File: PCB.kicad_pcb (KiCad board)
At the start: 2 copper layers, 60 x 60 mm, 51 parts, among them J1 USB_C_Receptacle_USB2.0_16P, J10 Conn_01x06_Socket, J11 Conn_01x02_Pin, J13 Conn_01x06_Pin, J2 Conn_01x06_Socket, J3 Conn_01x04_Pin, J4 Conn_01x06_Pin, J5 Conn_01x02_Pin, J6 Conn_01x02_Pin, J7 Conn_01x02_Pin, J8 Conn_01x04_Pin, J9 Conn_01x06_Pin, SW1 SW_Push, SW2 SW_Push, U1 TMC2209_SILENTSTEPSTICK, U2 USBLC6-2SC6, U4 AMS1117-3.3 (UMW), U5 TMC2209_SILENTSTEPSTICK, U6 ESP32-S3-WROOM-1

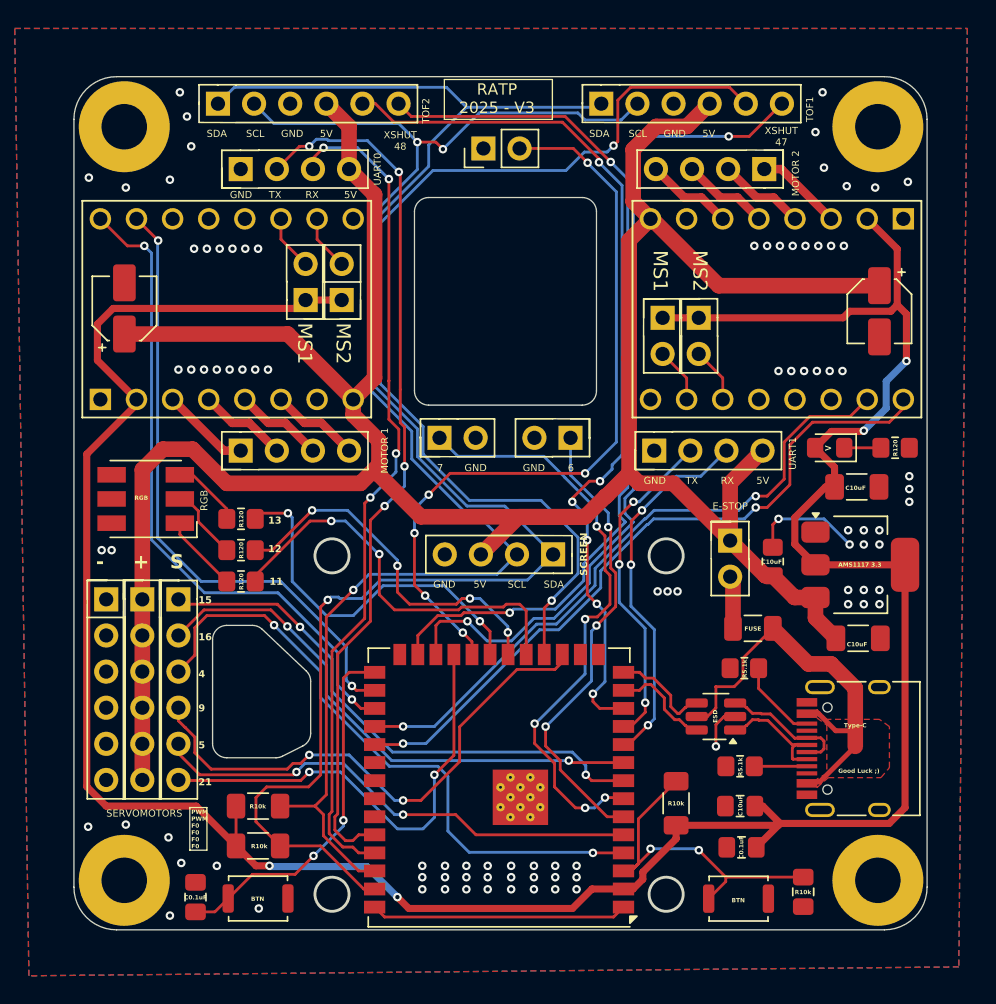
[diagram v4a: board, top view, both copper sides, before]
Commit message: fin routage + faire Trou Screen gnd
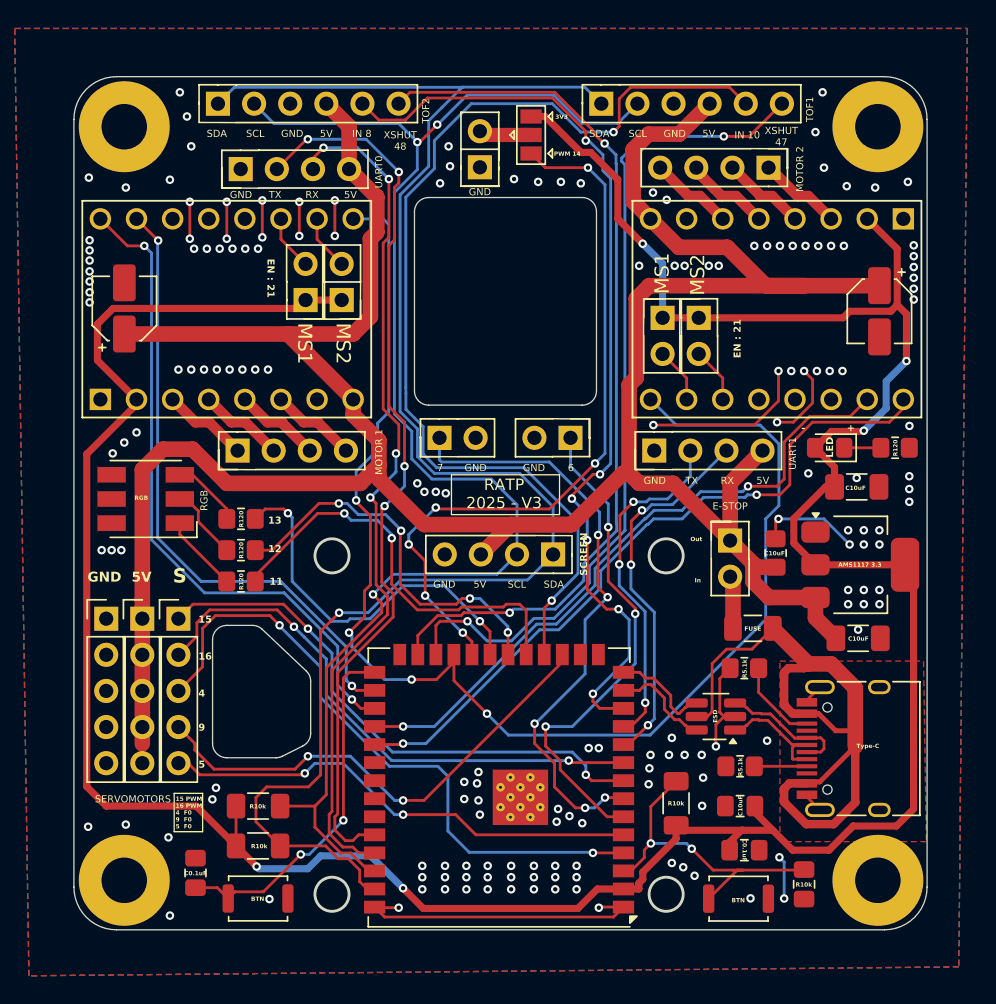
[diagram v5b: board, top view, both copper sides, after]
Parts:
- added JP5: SolderJumper_3_Open, Jumper:SolderJumper-3_P1.3mm_Open_Pad1.0x1.5mm, F.Cu at (145.4, 75.6)
- J13, J4, J9: value Conn_01x06_Pin -> Conn_01x05_Pin; footprint Connector_PinHeader_2.54mm:PinHeader_1x06_P2.54mm_Vertical -> Connector_PinHeader_2.54mm:PinHeader_1x05_P2.54mm_Vertical
- moved C1 1.70 mm to (121.8, 127.5)
- moved J13 1.36 mm to (115.5, 109.6)
- moved J4 1.36 mm to (120.6, 109.6)
- moved J9 1.36 mm to (118.1, 109.6)
- moved J11 1.35 mm to (141.8, 77.9), turned to 180 degrees
- moved C4 0.63 mm to (162.6, 105.0)
- moved C2 0.53 mm to (164.6, 128.3)
- moved J3 0.32 mm to (162.1, 77.9)
- moved C10 0.28 mm to (160.4, 125.9), turned to 0 degrees
- moved J8 0.22 mm to (124.8, 97.8)
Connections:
- J11 pad 2: GPIO14_PWM -> Net-(J11-Pin_2)
- U1 pad 16: GND -> GPIO21
- U5 pad 16: GND -> GPIO21
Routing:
- net GPIO21: track 32.3 -> 95.6 mm, vias 2 -> 4
- net GND: track 29.4 -> 72.8 mm, vias 93 -> 171
- net 3V3: track 198.2 -> 220.2 mm, vias 4 -> 5
- net VCC_5Vin: track 29.2 -> 48.0 mm
- net VCC_5V: track 192.1 -> 197.9 mm
- net Net-(J11-Pin_2): track 0.00 -> 3.71 mm
- net GPIO8: track 62.6 -> 65.7 mm
- net GPIO9: track 37.7 -> 34.7 mm
- net GPIO14_PWM: track 53.9 -> 51.7 mm
- net LAUNCHPULL: track 33.0 -> 35.2 mm
- net GPIO10: track 71.9 -> 73.3 mm
- net GPIO12_PWM: track 25.9 -> 27.3 mm
- net GPIO16_PWM: track 37.7 -> 39.1 mm
- net UART0+: track 59.6 -> 60.9 mm
- net UART0-: track 62.2 -> 63.4 mm
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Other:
- board text added: "15 PWM 16 PWM 4 F0 9 F0 5 F0"
- board text added: "3V3"
- board text added: "EN : 21"
- board text added: "IN 10"
- board text added: "IN 8"
- board text added: "In"
- board text added: "LED"
- board text added: "Out"
- board text added: "PWM 14"
- board text removed: "21"
- board text removed: ">"
- board text removed: "Good Luck ;)"
- board text removed: "PWM PWM F0 F0 F0 F0"

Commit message: test DRC V3 OK prod
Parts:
- C7: value 10uF -> 22uF
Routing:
- net GND: track 72.8 -> 97.8 mm, vias 171 -> 192
- net ESP32_EN: track 23.0 -> 27.2 mm
- net 3V3: track 220.2 -> 221.4 mm
- net VCC_5V: track 197.9 -> 198.9 mm
- net LAUNCHPULL: track 35.2 -> 34.4 mm
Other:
- board text added: "C100uF"
- board text added: "C22uF"
- board text added: "Check short circuit !"
- board text added: "Chicken Jockey"
- board text added: "Flint & Steel"
- board text added: "I AM STEVE"
- board text added: "POWER SUPPLY : PD Control 5V/3A POWER SUPPLY : using E-Stop MAX 3A STEPPER : MAX 2.40A/Phase +20°C UART : wired like TX on TX & RX on RX FUSE PPTC: hold 3A & drop 3.5A MULTI BOARD : use UART0 or UART1 UART0 : DON'T USE when flashing"
- board text added: "Unimakers Amiens"

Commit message: V3 Corrigée (ToF)
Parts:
- C7: value 22uF -> 10uF
- moved JP5 0.86 mm to (145.5, 76.5)
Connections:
- J10 pad 1: SDA -> VCC_5V
- J10 pad 2: SCL -> GND
- J10 pad 3: GND -> SCL
- J10 pad 4: VCC_5V -> SDA
- J2 pad 1: SDA -> VCC_5V
- J2 pad 2: SCL -> GND
- J2 pad 3: GND -> SCL
- J2 pad 4: VCC_5V -> SDA
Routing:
- net VCC_5V: track 198.9 -> 202.4 mm
- net GND: track 97.8 -> 100.4 mm, vias 192 -> 191
- net GPIO10: track 73.3 -> 71.0 mm
- net Net-(J11-Pin_2): track 3.71 -> 4.54 mm
- net SDA: track 117.0 -> 116.3 mm, vias 1 -> 2
- net XSHUT1: track 58.7 -> 58.2 mm, vias 2 -> 1
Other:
- board text added: "FUSE PPTC:hold 3A & drop 3.5A MULTI BOARD:use UART0/UART1 UART0:DON'T USE when flashing"
- board text added: "POWER SUPPLY:PD Control 5V/3A POWER SUPPLY:E-Stop MAX 3A STEPPER:MAX 2.40A/Phase +20°C UART:wired TX on TX/RX on RX FUSE PPTC:hold 3A&drop 3.5A"
- board text removed: "Chicken Jockey"
- board text removed: "Flint & Steel"
- board text removed: "I AM STEVE"
- board text removed: "POWER SUPPLY : PD Control 5V/3A POWER SUPPLY : using E-Stop MAX 3A STEPPER : MAX 2.40A/Phase +20°C UART : wired like TX on TX & RX on RX FUSE PPTC: hold 3A & drop 3.5A MULTI BOARD : use UART0 or UART1 UART0 : DON'T USE when flashing"

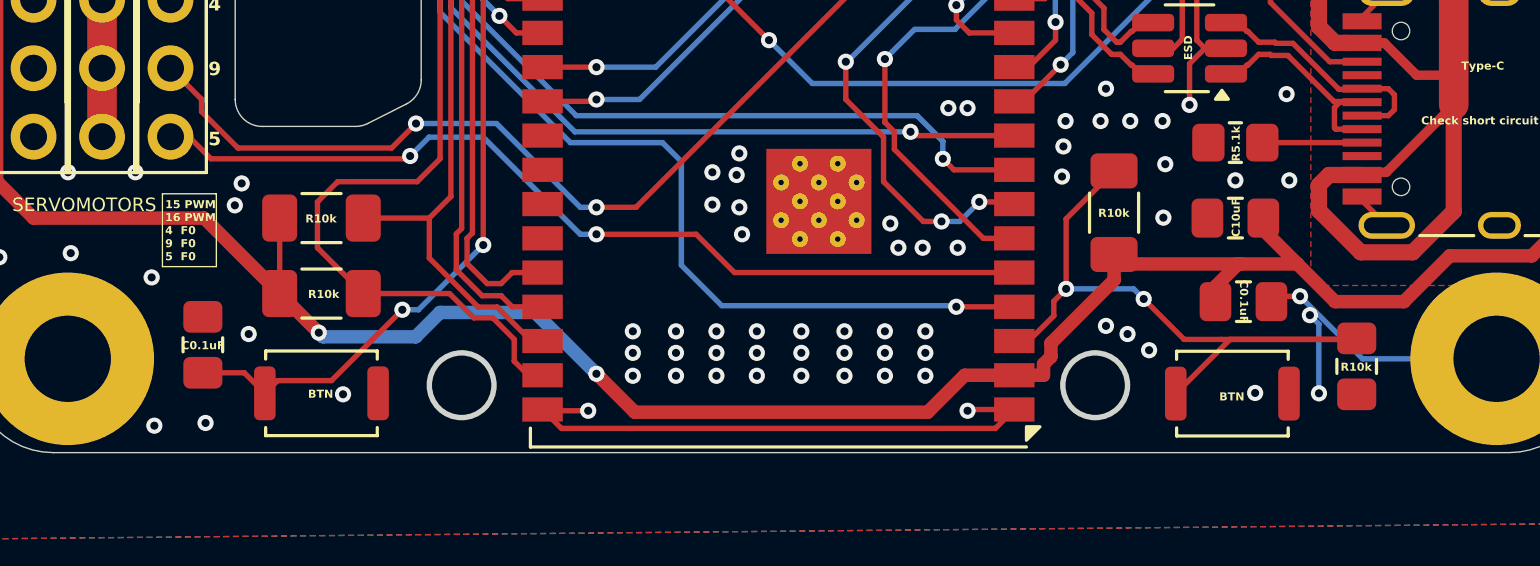
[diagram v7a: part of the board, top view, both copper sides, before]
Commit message: fix condo + sériegraphie
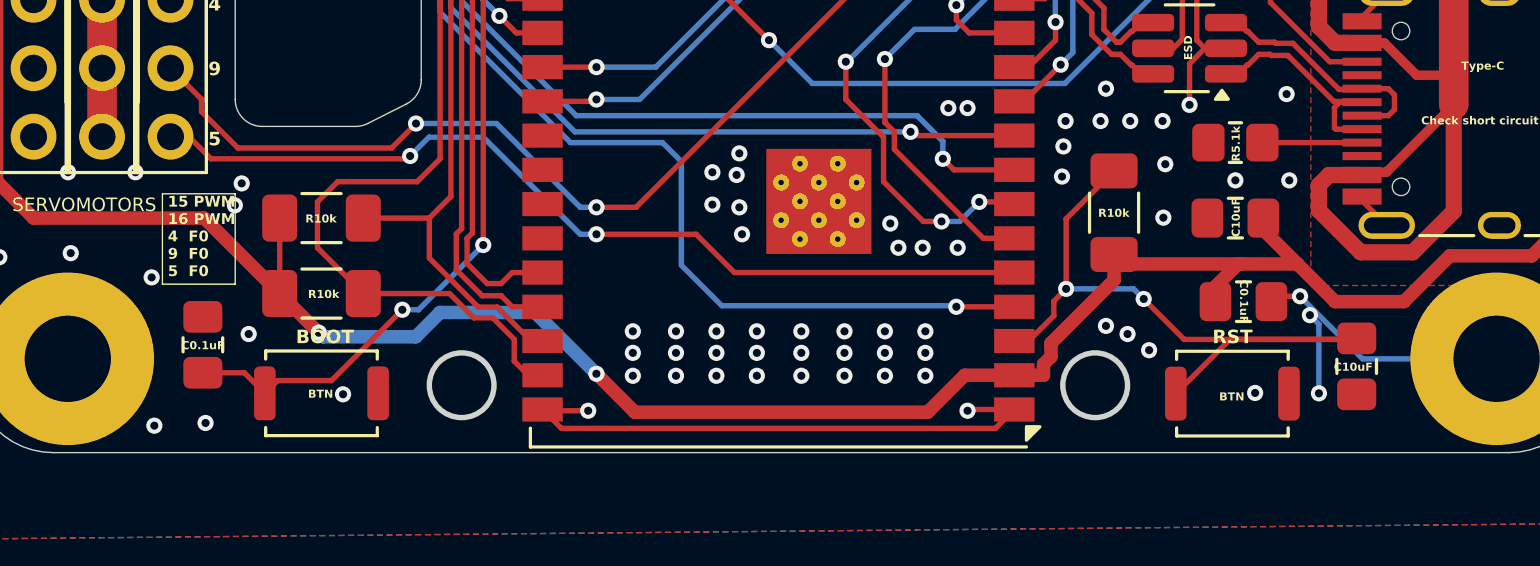
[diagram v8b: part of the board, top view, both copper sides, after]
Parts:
- C2: value 0.1uF -> 10uF
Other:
- board text added: "BOOT"
- board text added: "RST"
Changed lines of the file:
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@@
 			)
 		)
-		(property "Value" "0.1uF"
+		(property "Value" "10uF"
 			(at 0 1.68 90)
 			(layer "F.Fab")
@@
 	(gr_rect
 		(start 120.3 121.9)
-		(end 122.3 124.6)
+		(end 123 125.25)
 		(stroke
 			(width 0.05)
@@
 	)
 	(gr_text "15 PWM\n16 PWM\n4  F0\n9  F0\n5  F0"
-		(at 120.4 124.4 0)
+		(at 120.5 125 0)
 		(layer "F.SilkS")
 		(effects
 			(font
-				(size 0.3 0.3)
+				(size 0.4 0.4)
 				(thickness 0.05)
 				(bold yes)
@@
 		)
 	)
-	(gr_text "R10k"
-		(at 164 128.5 0)
+	(gr_text "C10uF"
+		(at 163.75 128.5 0)
 		(layer "F.SilkS")
 		(effects
@@
 		)
 	)
+	(gr_text "BOOT"
+		(at 125.25 127.5 0)
+		(layer "F.SilkS")
+		(effects
+			(font
+				(size 0.5 0.5)
+				(thickness 0.125)
+				(bold yes)
+			)
+			(justify left bottom)
+		)
+	)
 	(gr_text "-"
 		(at 166.4 96.5 90)
@@
 				(bold yes)
 			)
+			(justify left bottom)
+		)
+	)
+	(gr_text "RST"
+		(at 159.25 127.5 0)
+		(layer "F.SilkS")
+		(effects
+			(font
+				(size 0.5 0.5)
+				(thickness 0.125)
+				(bold yes)
+			)
